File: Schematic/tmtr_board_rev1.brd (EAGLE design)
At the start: 70 x 41 mm, 25 parts, among them IC1 MEGA8-AI, J1 POWER_JACKPTH_LOCK

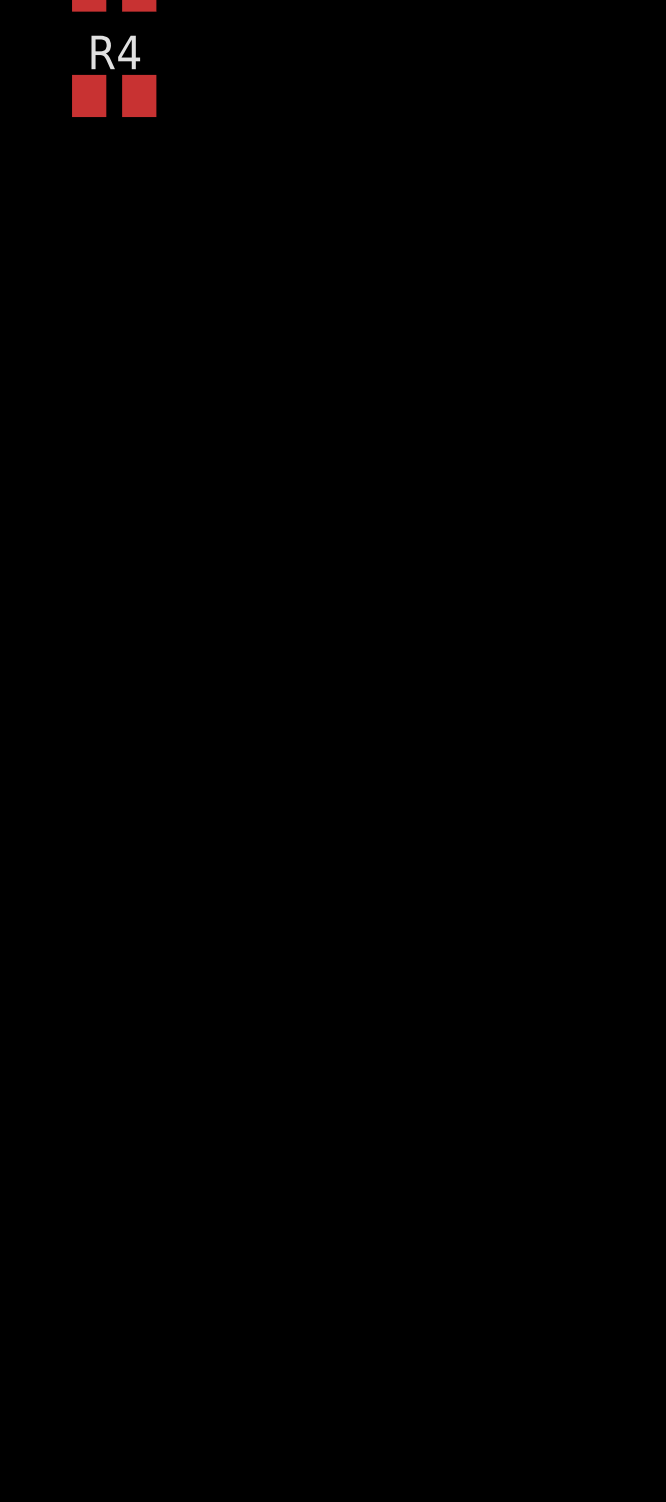
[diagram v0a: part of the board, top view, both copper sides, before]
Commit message: 
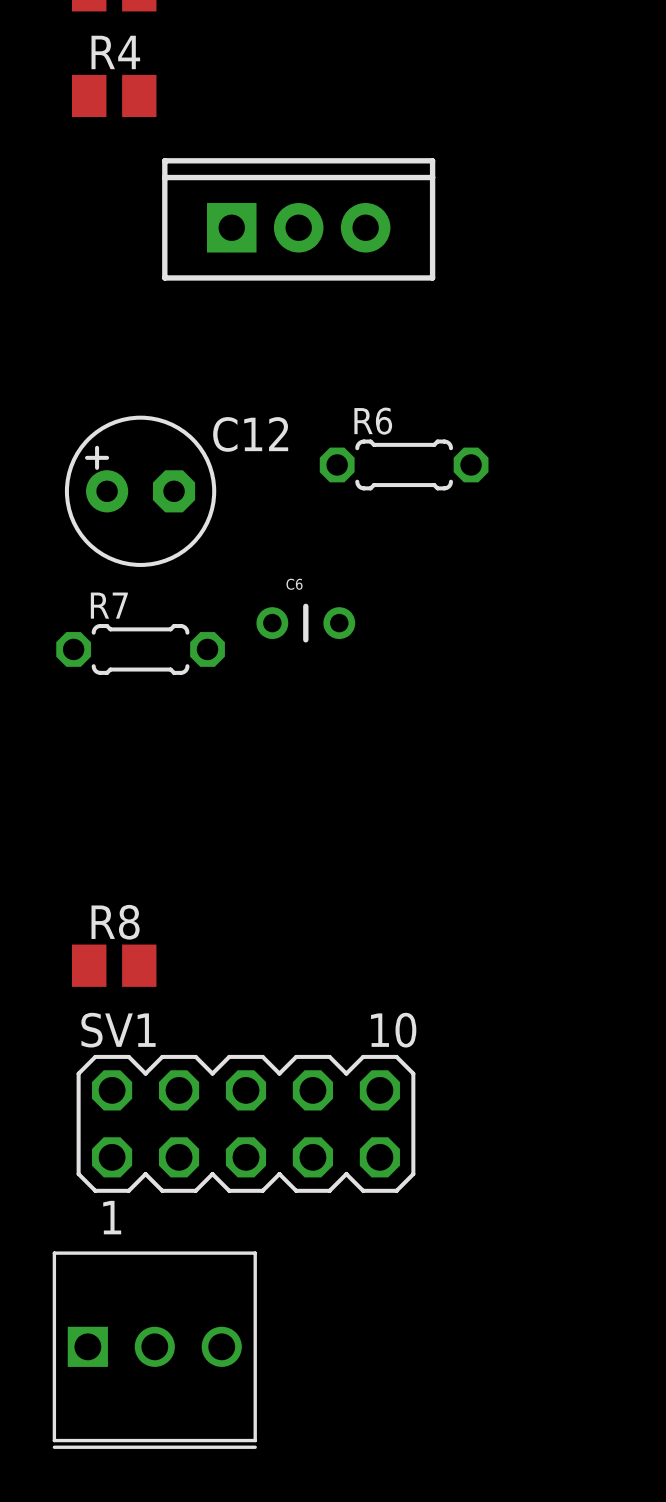
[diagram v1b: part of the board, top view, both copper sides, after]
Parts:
- added C12: (no value), rcl:E2,5-6
- added C6: (no value), SparkFun1:CAP-PTH-SMALL
- added POT1: POT100K_3362U, SparkFun5:3362U
- added R6, R7: (no value), resistor:0204/5
- added R8: (no value), resistor:M0805
- added SV1: (no value), con-lstb:MA05-2
- added U6: V_REG_317SINK, SparkFun4:TO220-ADJ
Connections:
- new net 3.3V: R7.1, U6.OUT
- new net 5V\: POT1.P$1
- new net DB4: IC1.2
- new net DB5: IC1.9, SV1.2
- new net DB6: IC1.10, SV1.4
- new net DB7: IC1.11, SV1.6
- new net EN: IC1.32
- new net N$13: POT1.P$2, SV1.1
- new net N$20: R6.2, R7.2, U6.ADJ
- new net N$21: C12.+, C6.2
- new net N$9: IC1.30, R8.2, SW1.3, SW1.4
- new net R/W: IC1.31
- new net RS: IC1.1
- net 5V: now also R8.1, SV1.10, U6.IN
- net GND: now also C12.-, C6.1, POT1.P$3, R6.1, SV1.8, SW1.1, SW1.2
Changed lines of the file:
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@@
 <element name="R3" library="resistor" package="M0805" value="" x="2" y="-47"/>
 <element name="R4" library="resistor" package="M0805" value="" x="2" y="-51"/>
+<element name="U6" library="SparkFun4" package="TO220-ADJ" value="V_REG_317SINK" x="9" y="-56"/>
+<element name="R6" library="resistor" package="0204/5" value="" x="13" y="-65"/>
+<element name="R7" library="resistor" package="0204/5" value="" x="3" y="-72"/>
+<element name="C6" library="SparkFun1" package="CAP-PTH-SMALL" value="" x="8" y="-71"/>
+<element name="C12" library="rcl" package="E2,5-6" value="" x="3" y="-66"/>
+<element name="R8" library="resistor" package="M0805" value="" x="2" y="-84"/>
+<element name="SV1" library="con-lstb" package="MA05-2" value="" x="7" y="-90">
+<attribute name="OC_NEWARK" value="unknown" x="7" y="-90" size="1.778" layer="27" display="off"/>
+<attribute name="MPN" value="" x="7" y="-90" size="1.778" layer="27" display="off"/>
+<attribute name="MF" value="" x="7" y="-90" size="1.778" layer="27" display="off"/>
+<attribute name="OC_FARNELL" value="unknown" x="7" y="-90" size="1.778" layer="27" display="off"/>
+</element>
+<element name="POT1" library="SparkFun5" package="3362U" value="POT100K_3362U" x="1" y="-101"/>
 </elements>
 <signals>
@@
 <contactref element="J2" pad="1"/>
 <contactref element="R3" pad="2"/>
-<wire x1="51.38" y1="30.29" x2="51.38" y2="31.7626" width="0" layer="19" extent="16-16"/>
-<wire x1="37.1618" y1="27.8782" x2="45.19" y2="34.75" width="0" layer="19" extent="2-16"/>
-<wire x1="27.11" y1="32.14" x2="34.51" y2="30.53" width="0" layer="19" extent="16-16"/>
-<wire x1="8.2" y1="14.7" x2="10.49" y2="20.44" width="0" layer="19" extent="16-16"/>
+<contactref element="R6" pad="1"/>
+<contactref element="C6" pad="1"/>
+<contactref element="C12" pad="-"/>
+<contactref element="SW1" pad="1"/>
+<contactref element="SW1" pad="2"/>
+<contactref element="SV1" pad="8"/>
+<contactref element="POT1" pad="P$3"/>
+<wire x1="9.54" y1="-88.73" x2="6.08" y2="-98.46" width="0" layer="19" extent="1-1"/>
+<wire x1="8" y1="-71" x2="9.54" y2="-88.73" width="0" layer="19" extent="1-1"/>
+<wire x1="4.27" y1="-66" x2="8" y2="-71" width="0" layer="19" extent="1-1"/>
+<wire x1="10.46" y1="-65" x2="4.27" y2="-66" width="0" layer="19" extent="1-1"/>
+<wire x1="2.95" y1="-47" x2="4.27" y2="-66" width="0" layer="19" extent="1-1"/>
+<wire x1="6.27" y1="-29.08" x2="2.95" y2="-47" width="0" layer="19" extent="1-1"/>
+<wire x1="6.27" y1="-26.54" x2="6.27" y2="-29.08" width="0" layer="19" extent="1-1"/>
+<wire x1="6.27" y1="-24" x2="6.27" y2="-26.54" width="0" layer="19" extent="1-1"/>
+<wire x1="6.27" y1="-21.46" x2="6.27" y2="-24" width="0" layer="19" extent="1-1"/>
+<wire x1="4.73" y1="-15" x2="6.27" y2="-21.46" width="0" layer="19" extent="1-1"/>
+<wire x1="2.19" y1="-15" x2="4.73" y2="-15" width="0" layer="19" extent="1-1"/>
+<wire x1="9.0324" y1="7.3676" x2="4.73" y2="-15" width="0" layer="19" extent="16-16"/>
 <wire x1="10.97" y1="7.3676" x2="9.0324" y2="7.3676" width="0" layer="19" extent="16-16"/>
-<wire x1="4.73" y1="-15" x2="9.0324" y2="7.3676" width="0" layer="19" extent="16-16"/>
-<wire x1="2.19" y1="-15" x2="4.73" y2="-15" width="0" layer="19" extent="1-1"/>
-<wire x1="6.27" y1="-21.46" x2="4.73" y2="-15" width="0" layer="19" extent="1-1"/>
-<wire x1="6.27" y1="-24" x2="6.27" y2="-21.46" width="0" layer="19" extent="1-1"/>
-<wire x1="6.27" y1="-26.54" x2="6.27" y2="-24" width="0" layer="19" extent="1-1"/>
-<wire x1="6.27" y1="-29.08" x2="6.27" y2="-26.54" width="0" layer="19" extent="1-1"/>
-<wire x1="2.95" y1="-47" x2="6.27" y2="-29.08" width="0" layer="19" extent="1-1"/>
+<wire x1="10.49" y1="20.44" x2="8.2" y2="14.7" width="0" layer="19" extent="16-16"/>
+<wire x1="30.6788" y1="27.2306" x2="26.18" y2="31.21" width="0" layer="19" extent="16-16"/>
+<wire x1="33.93" y1="25.87" x2="30.6788" y2="27.2306" width="0" layer="19" extent="16-16"/>
+<wire x1="37.1812" y1="27.2306" x2="37.1618" y2="27.25" width="0" layer="19" extent="16-16"/>
+<wire x1="45.19" y1="34.75" x2="37.1618" y2="27.8782" width="0" layer="19" extent="2-16"/>
+<wire x1="51.38" y1="31.7626" x2="51.38" y2="30.29" width="0" layer="19" extent="16-16"/>
 </signal>
 <signal name="5V">
@@
 <wire x1="50.27" y1="17.3" x2="48.69" y2="17.3" width="0.4064" layer="16"/>
 <contactref element="R2" pad="1"/>
-<wire x1="50.27" y1="17.3" x2="63.31" y2="13.82" width="0" layer="19" extent="16-16"/>
-<wire x1="39.81" y1="25.44" x2="48.69" y2="17.3" width="0" layer="19" extent="16-16"/>
+<contactref element="U6" pad="IN"/>
+<contactref element="R8" pad="1"/>
+<contactref element="SV1" pad="10"/>
+<wire x1="12.08" y1="-88.73" x2="1.05" y2="-84" width="0" layer="19" extent="1-1"/>
+<wire x1="11.54" y1="-56" x2="1.05" y2="-84" width="0" layer="19" extent="1-1"/>
+<wire x1="4.04" y1="17.94" x2="11.54" y2="-56" width="0" layer="19" extent="16-16"/>
 <wire x1="5.45" y1="27.85" x2="5.4" y2="25.32" width="0" layer="19" extent="16-16"/>
+<wire x1="48.69" y1="17.3" x2="39.81" y2="25.44" width="0" layer="19" extent="16-16"/>
+<wire x1="63.31" y1="13.82" x2="50.27" y2="17.3" width="0" layer="19" extent="1-16"/>
 </signal>
 <signal name="N$12">
@@
 <wire x1="2.95" y1="-51" x2="48.98" y2="23.1774" width="0" layer="19" extent="1-16"/>
 </signal>
+<signal name="3.3V">
+<contactref element="U6" pad="OUT"/>
+<contactref element="R7" pad="1"/>
+<wire x1="9" y1="-56" x2="0.46" y2="-72" width="0" layer="19" extent="1-1"/>
+</signal>
+<signal name="N$20">
+<contactref element="R7" pad="2"/>
+<contactref element="U6" pad="ADJ"/>
+<contactref element="R6" pad="2"/>
+<wire x1="15.54" y1="-65" x2="5.54" y2="-72" width="0" layer="19" extent="1-1"/>
+<wire x1="6.46" y1="-56" x2="15.54" y2="-65" width="0" layer="19" extent="1-1"/>
+</signal>
+<signal name="N$21">
+<contactref element="C6" pad="2"/>
+<contactref element="C12" pad="+"/>
+<wire x1="10.54" y1="-71" x2="1.73" y2="-66" width="0" layer="19" extent="1-1"/>
+</signal>
+<signal name="DB7">
+<contactref element="IC1" pad="11"/>
+<contactref element="SV1" pad="6"/>
+<wire x1="7" y1="-88.73" x2="55.2726" y2="28.67" width="0" layer="19" extent="16-16"/>
+</signal>
+<signal name="DB6">
+<contactref element="IC1" pad="10"/>
+<contactref element="SV1" pad="4"/>
+<wire x1="55.2726" y1="29.47" x2="4.46" y2="-88.73" width="0" layer="19" extent="16-16"/>
+</signal>
+<signal name="DB5">
+<contactref element="IC1" pad="9"/>
+<contactref element="SV1" pad="2"/>
+<wire x1="55.2726" y1="30.27" x2="1.92" y2="-88.73" width="0" layer="19" extent="16-16"/>
+</signal>
+<signal name="DB4">
+<contactref element="IC1" pad="2"/>
+</signal>
+<signal name="RS">
+<contactref element="IC1" pad="1"/>
+</signal>
+<signal name="EN">
+<contactref element="IC1" pad="32"/>
+</signal>
+<signal name="R/W">
+<contactref element="IC1" pad="31"/>
+</signal>
+<signal name="N$9">
+<contactref element="R8" pad="2"/>
+<contactref element="SW1" pad="4"/>
+<contactref element="SW1" pad="3"/>
+<contactref element="IC1" pad="30"/>
+<wire x1="30.6788" y1="22.7094" x2="2.95" y2="-84" width="0" layer="19" extent="1-1"/>
+<wire x1="37.1812" y1="22.7094" x2="30.6788" y2="22.7094" width="0" layer="19" extent="1-1"/>
+<wire x1="46.6874" y1="28.67" x2="37.1812" y2="22.7094" width="0" layer="19" extent="16-16"/>
+</signal>
+<signal name="5V\">
+<contactref element="POT1" pad="P$1"/>
+</signal>
+<signal name="N$13">
+<contactref element="POT1" pad="P$2"/>
+<contactref element="SV1" pad="1"/>
+<wire x1="1.92" y1="-91.27" x2="3.54" y2="-98.46" width="0" layer="19" extent="1-1"/>
+</signal>
 </signals>

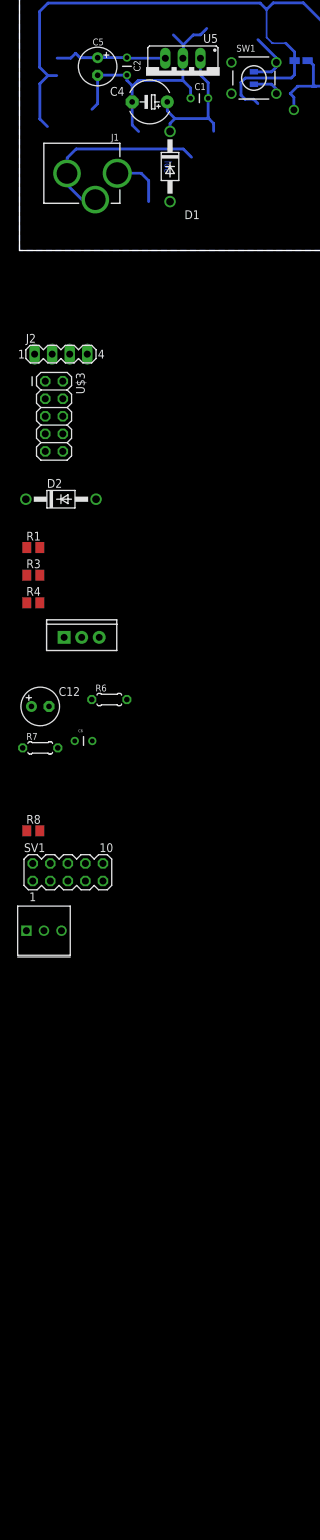
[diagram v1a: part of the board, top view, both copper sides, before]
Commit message: 
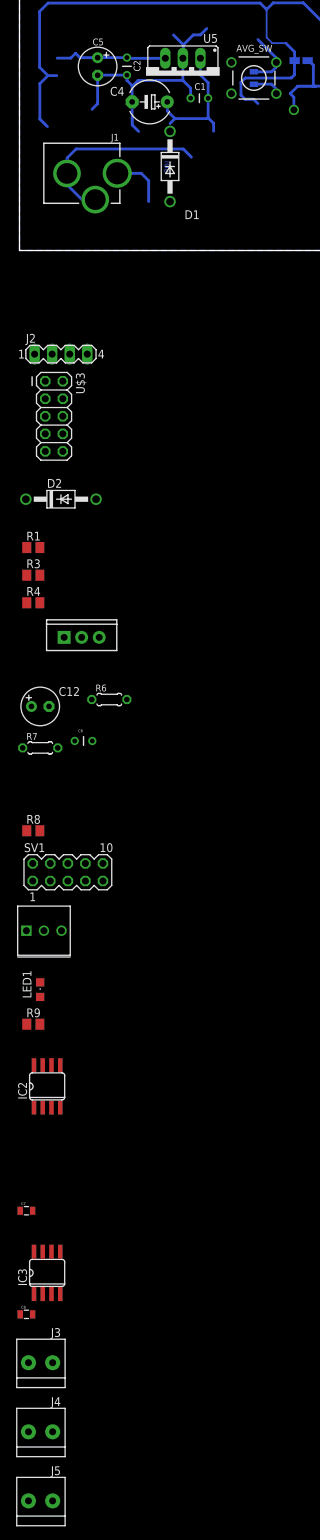
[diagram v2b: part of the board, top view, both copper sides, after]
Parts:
- added C7, C8: (no value), SparkFun1:0805
- added IC2, IC3: MAX31855, adafruit:SO08
- added J3, J4, J5: 1X2-3.5MM, adafruit:1X2-3.5MM
- added LED1: (no value), led:CHIPLED_0805
- added R9: (no value), resistor:M0805
- renumbered SW1 to AVG_SW
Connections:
- removed net 5V\: POT1.P$1
- removed net N$21: C12.+, C6.2
- removed net N$8: C13.2, IC1.6
- new net CS_TS_IC0: IC1.27, IC2.6
- new net CS_TS_IC1: IC1.13, IC3.6
- new net DO_TS_IC0: IC1.26, IC2.7
- new net DO_TS_IC1: IC1.12, IC3.7
- new net LED2: IC1.25, LED2.A
- new net N$10: LED1.C, R9.2
- new net SCK_TS_IC0: IC1.28, IC2.5
- new net SCK_TS_IC1: IC1.14, IC3.5
- new net T+0: IC2.3, J3.1
- new net T+1: IC3.3, J4.1
- new net T-0: IC2.2, J3.2
- new net T-1: IC3.2, J4.2
- net 3.3V: now also C12.+, C6.2, C7.1, C8.1, IC2.4, IC3.4
- net 5V: now also C11.2, C13.2, IC1.4, IC1.6, POT1.P$1, R9.1
- net GND: now also C7.2, C8.2, IC2.1, IC3.1
- net LED1: now also IC1.24, LED1.A; no longer LED2.A
- net N$4: now also D1.C, D2.C, J5.1; no longer C11.2, IC1.4
- net VIN: now also J5.2; no longer D1.C, D2.C
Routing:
- net VIN: track 21.3 -> 20.2 mm

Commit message: 
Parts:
- removed AVG_SW: (no value), SparkFun1:TACTILE-PTH
- removed C14, C15: (no value), SparkFun1:0805
- removed IC1: MEGA8-AI, atmel:TQFP32-08
- removed IC2, IC3: MAX31855, adafruit:SO08
- removed LED1, LED2: (no value), led:CHIPLED_0805
- removed POT1: POT100K_3362U, SparkFun5:3362U
- removed SV1: (no value), con-lstb:MA05-2
- removed U$3: AVR_SPI_PROG, SparkFun2:AVR_ICSP
- removed U6: V_REG_317SINK, SparkFun4:TO220-ADJ
- added C10, C9: (no value), SparkFun1:0805
- added J6: AVR_SPI_PROG, SparkFun2:AVR_ICSP
- added J7, J8: 22-23-2021, con-molex:22-23-2021
- added LED3, LED4: (no value), led:CHIPLED_0805
- added R10, R11: (no value), resistor:M0805
- added U1: (no value), v-reg:78XXS
- added U2: LD117AS12TR, v-reg:SOT223
- added U3: MEGA8-AI, atmel:TQFP32-08
- added U4: MAX31855, adafruit:SO08
- C1: device SparkFun1:CAP-PTH-SMALL -> rcl:E5-6
- C12: device rcl:E2,5-6 -> SparkFun1:0805
- C3: device SparkFun1:0805 -> rcl:E2,5-6
- C4: device rcl:E5-6 -> SparkFun1:CAP-PTH-SMALL
- D1, D2: value 1N4004 -> (none); device diode:DO41-10 -> semicon-smd-ipc:SMB
- J1: value POWER_JACKPTH_LOCK -> 22-23-2021; device SparkFun4:POWER_JACK_PTH_LOCK -> con-molex:22-23-2021
- J2: value (none) -> POWER_JACKPTH_LOCK; device con-lstb:MA04-1 -> SparkFun4:POWER_JACK_PTH_LOCK
- J3: value 1X2-3.5MM -> (none); device adafruit:1X2-3.5MM -> con-lstb:MA04-1
- J4: value 1X2-3.5MM -> 22-23-2021; device adafruit:1X2-3.5MM -> con-molex:22-23-2021
- J5: value 1X2-3.5MM -> (none); device adafruit:1X2-3.5MM -> con-lstb:MA05-2
- R6, R7: device resistor:0204/5 -> resistor:M0805
- U5: value (none) -> MAX31855; device v-reg:78XXS -> adafruit:SO08
- moved J5 243.2 mm to (42.1, 59.1), turned to 90 degrees
- moved C8 197.3 mm to (27.6, 41.5), turned to 90 degrees
- moved J4 189.6 mm to (27.3, 17.0)
- moved C7 189.1 mm to (41.7, 45.7), turned to 180 degrees
- moved J3 176.2 mm to (6.47, 15.1)
- moved C6 141.5 mm to (16.9, 70.2)
- moved R9 138.1 mm to (25.7, 24.1), turned to 90 degrees
- moved R8 130.3 mm to (35.1, 42.1), turned to 270 degrees
- moved R7 119.7 mm to (21.7, 46.3)
- moved R6 110.3 mm to (41.4, 41.6)
- moved C12 103.8 mm to (36.5, 32.2), turned to 90 degrees
- moved R1 100.3 mm to (17.4, 56.1)
- moved R4 91.6 mm to (17.7, 39.3), turned to 180 degrees
- moved R3 84.3 mm to (18.4, 35.7)
- moved R2 59.9 mm to (17.6, 53.5), turned to 0 degrees
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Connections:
- net 3.3V: now also C12.1, C13.1, C5.+, R1.2, U2.4, U4.4, U5.4; no longer C12.+, C7.1, C8.1, IC2.4, IC3.4, R7.1, U6.OUT
- net 5V: now also C10.2, C3.+, C4.2, J5.10, R10.1, R6.1, U1.OUT, U2.3, U3.4, U3.6; no longer C13.2, C2.2, C5.+, IC1.4, IC1.6, POT1.P$1, R2.1, SV1.10, U5.OUT, U6.IN
- net CS_TS_IC0: now also U3.27, U4.6; no longer IC1.27, IC2.6
- net CS_TS_IC1: now also U3.13, U5.6; no longer IC1.13, IC3.6
- net DB4: now also J5.5, U3.2; no longer IC1.2
- net DB5: now also J5.2, U3.9; no longer IC1.9, SV1.2
- net DB6: now also J5.4, U3.10; no longer IC1.10, SV1.4
- net DB7: now also J5.6, U3.11; no longer IC1.11, SV1.6
- net DO_TS_IC0: now also U3.26, U4.7; no longer IC1.26, IC2.7
- net DO_TS_IC1: now also U3.12, U5.7; no longer IC1.12, IC3.7
- net EN: now also J5.9, U3.32; no longer IC1.32
- net GND: now also C1.-, C10.1, C12.2, C13.2, C3.-, C4.1, C7.1, J2.GND, J2.GNDBREAK, J3.1, J3.2, J4.2, J5.8, J6.10, J6.4, J6.6, J6.8, R11.2, R2.2, R4.2, U1.GND, U3.3, U3.5, U4.1, U5.1; no longer AVG_SW.1, AVG_SW.2, C1.1, C12.-, C13.1, C3.1, C4.-, C7.2, C8.2, IC1.3, IC1.5, IC2.1, IC3.1, J1.GND, J1.GNDBREAK, J2.1, J2.2, POT1.P$3, R3.2, R6.1, SV1.8, U$3.10, U$3.4, U$3.6, U$3.8, U5.GND
- net LED1: now also LED4.C, U3.24; no longer IC1.24, LED1.A
- net LED2: now also LED3.C, U3.25; no longer IC1.25, LED2.A
- net N$1: now also D1.2, J2.PWR; no longer D1.A, J1.PWR
- net N$10: now also LED4.A, R8.2; no longer LED1.C, R9.2
- net N$12: now also LED3.A, R6.2; no longer LED2.C, R2.2
- net N$13: now also J5.1, R10.2, R11.1; no longer POT1.P$2, SV1.1
- net N$2: now also D2.2, J3.3, J3.4; no longer D2.A, J2.3, J2.4
- net N$20: now also R1.1, R2.1, U2.1; no longer R6.2, R7.2, U6.ADJ
- net N$3: now also R7.2, U3.19; no longer IC1.23, R4.2
- net N$4: now also D1.1, D2.1, J1.1; no longer D1.C, D2.C, J5.1
- net N$5: now also C8.2, U3.20; no longer C14.2, IC1.20
- net N$6: now also C9.2, U3.18; no longer C15.2, IC1.18
- net N$7: now also C8.1, C9.1, U3.21; no longer C14.1, C15.1, IC1.21
- net N$9: now also J4.1, R9.2, U3.30; no longer AVG_SW.3, AVG_SW.4, IC1.30, R8.2
- net R/W: now also J5.3, U3.31; no longer IC1.31
- net RS: now also J5.7, U3.1; no longer IC1.1
- net SCK_TS_IC0: now also U3.28, U4.5; no longer IC1.28, IC2.5
- net SCK_TS_IC1: now also U3.14, U5.5; no longer IC1.14, IC3.5
- net T+0: now also J7.2, U4.3; no longer IC2.3, J3.1
- net T+1: now also J8.2, U5.3; no longer IC3.3, J4.1
- net T-0: now also J7.1, U4.2; no longer IC2.2, J3.2
- net T-1: now also J8.1, U5.2; no longer IC3.2, J4.2
- net UC-MISO: now also J6.9, U3.16; no longer IC1.16, U$3.9
- net UC-MOSI: now also J6.1, U3.15; no longer IC1.15, U$3.1
- net UC-RST: now also C7.2, J6.5, U3.29; no longer C3.2, IC1.29, U$3.5
- net UC-SCK: now also J6.7, U3.17; no longer IC1.17, U$3.7
- net VIN: now also C1.+, C2.2, J1.2, R3.1, U1.IN; no longer C1.2, C4.+, J5.2, R1.1, U5.IN
- net VIN_SENSE: now also R3.2, R7.1; no longer R1.2, R3.1
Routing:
- net GND: track 144.5 -> 0.00 mm, vias 2 -> 0
- net 5V: track 121.4 -> 0.00 mm, vias 2 -> 0
- net VIN: track 20.2 -> 0.00 mm
- net UC-RST: track 19.0 -> 0.00 mm, vias 1 -> 0
- net N$12: track 11.6 -> 0.00 mm
- net N$1: track 8.03 -> 0.00 mm
- removed copper zone on layer 16, net GND
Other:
- board size 70 x 41 mm -> 50 x 80 mm
- board text removed: "sol"
